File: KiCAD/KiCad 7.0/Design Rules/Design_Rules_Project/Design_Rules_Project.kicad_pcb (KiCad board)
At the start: 2 copper layers, 34 x 31 mm, 2 parts, among them J1 2.54mm spaced headers, J2 1mm diameter

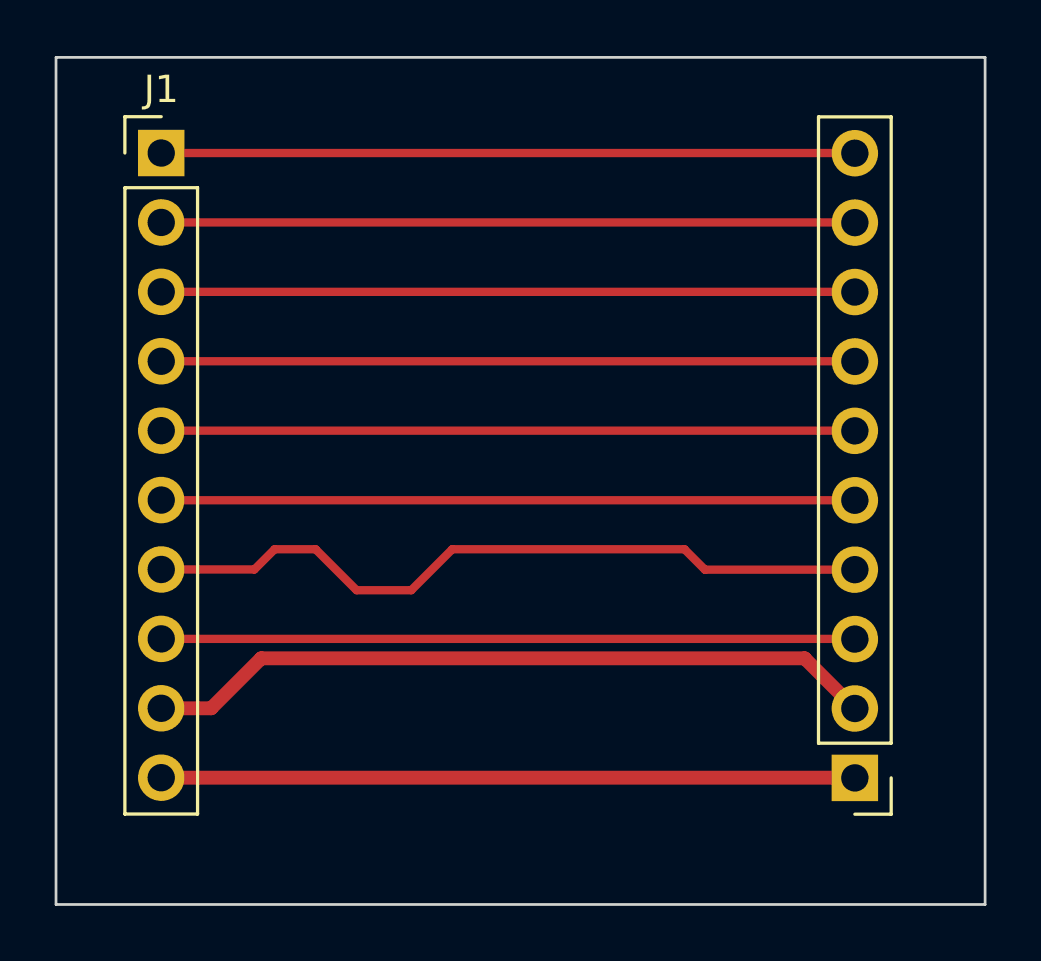
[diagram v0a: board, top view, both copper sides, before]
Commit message: Fix clearance with fill zones
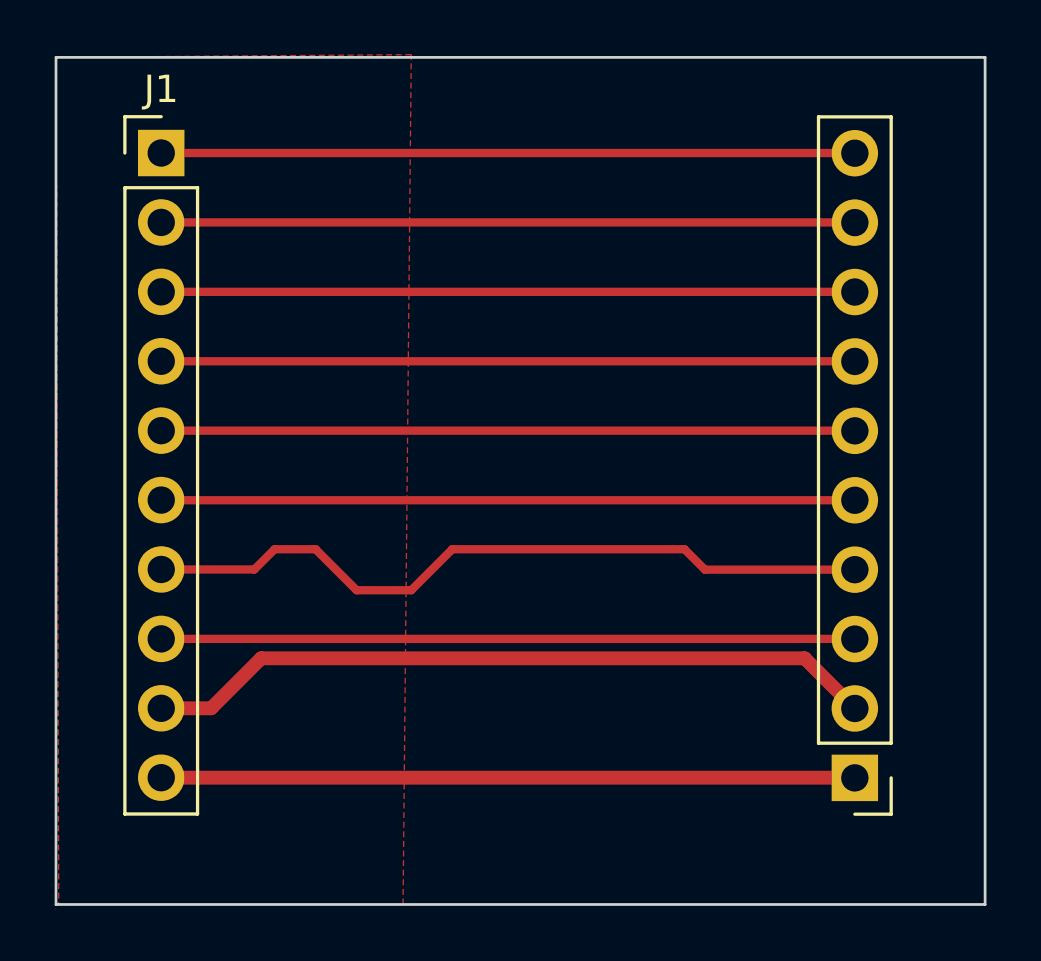
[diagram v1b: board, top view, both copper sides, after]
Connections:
- net Net-(J1-Pin_10) renamed GND
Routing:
- added copper zone on F.Cu, net GND
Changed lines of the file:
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@@
   (net 8 "Net-(J1-Pin_8)")
   (net 9 "Net-(J1-Pin_9)")
-  (net 10 "Net-(J1-Pin_10)")
+  (net 10 "GND")
   (footprint "Connector_PinHeader_2.54mm:PinHeader_1x10_P2.54mm_Vertical" (layer "F.Cu")
     (at 69.35 66)
@@
       (net 9 "Net-(J1-Pin_9)") (pinfunction "Pin_9") (pintype "passive"))
     (pad "10" thru_hole oval (at 0 22.86) (size 1.7 1.7) (drill 1) (layers "*.Cu" "*.Mask")
-      (net 10 "Net-(J1-Pin_10)") (pinfunction "Pin_10") (pintype "passive"))
+      (net 10 "GND") (pinfunction "Pin_10") (pintype "passive"))
     (model "${KICAD6_3DMODEL_DIR}/Connector_PinHeader_2.54mm.3dshapes/PinHeader_1x10_P2.54mm_Vertical.wrl"
       (offset (xyz 0 0 0))
@@
       (stroke (width 0.1) (type solid)) (layer "F.Fab"))
     (pad "1" thru_hole rect (at 0 0 180) (size 1.7 1.7) (drill 1) (layers "*.Cu" "*.Mask")
-      (net 10 "Net-(J1-Pin_10)") (pinfunction "Pin_1") (pintype "passive"))
+      (net 10 "GND") (pinfunction "Pin_1") (pintype "passive"))
     (pad "2" thru_hole oval (at 0 2.54 180) (size 1.7 1.7) (drill 1) (layers "*.Cu" "*.Mask")
       (net 9 "Net-(J1-Pin_9)") (pinfunction "Pin_2") (pintype "passive"))
@@
   (segment (start 94.726633 88.86) (end 94.733503 88.86687) (width 0.508) (layer "F.Cu") (net 10))
   (segment (start 69.35 88.86) (end 94.726633 88.86) (width 0.508) (layer "F.Cu") (net 10))
+  (zone (net 10) (net_name "GND") (layer "F.Cu") (hatch edge 0.5)
+    (connect_pads (clearance 0.7))
+    (min_thickness 0.25) (filled_areas_thickness no)
+    (fill yes (thermal_gap 0.5) (thermal_bridge_width 0.5))
+    (polygon
+      (pts
+        (xy 65.5 62.5)
+        (xy 65.6 93.5)
+        (xy 78.2 93.5)
+        (xy 78.5 62.4)
+      )
+    )
+  )
 )
